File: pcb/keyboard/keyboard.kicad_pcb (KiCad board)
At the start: 2 copper layers, 125.5 x 94.2 mm, 62 parts

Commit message: imp: pcb design change
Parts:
- added REF**: TC24CA, Button_Switch_SMD:TC24CA, F.Cu at (259.1, 106.5)
- added REF**: TC24CA, Button_Switch_SMD:TC24CA, B.Cu at (259.1, 106.5)
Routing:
- net P7: track 17.5 -> 24.8 mm, vias 1 -> 2
- net P9: track 58.1 -> 54.4 mm
- net GND: track 95.3 -> 96.9 mm
- net BAT: track 70.6 -> 70.9 mm, vias 3 -> 5

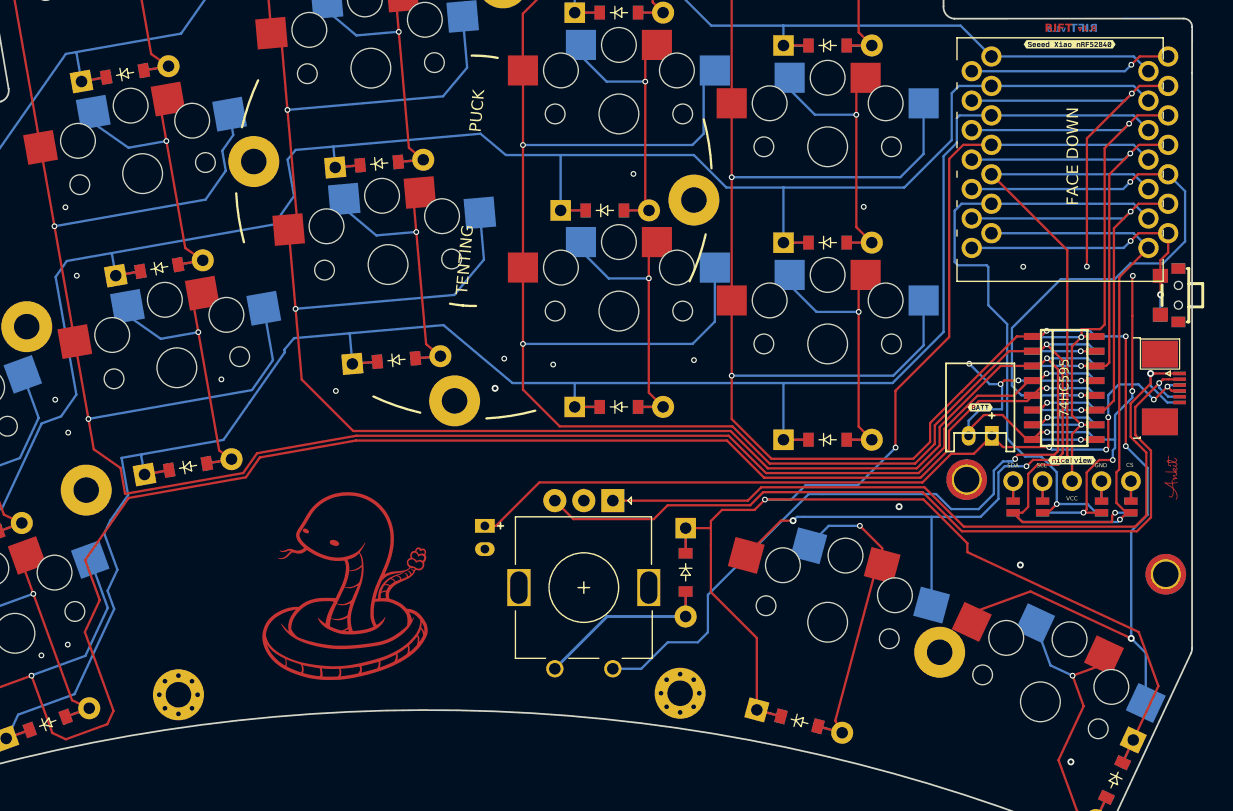
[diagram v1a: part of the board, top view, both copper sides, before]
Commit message: add: i2c resistor pull resistor
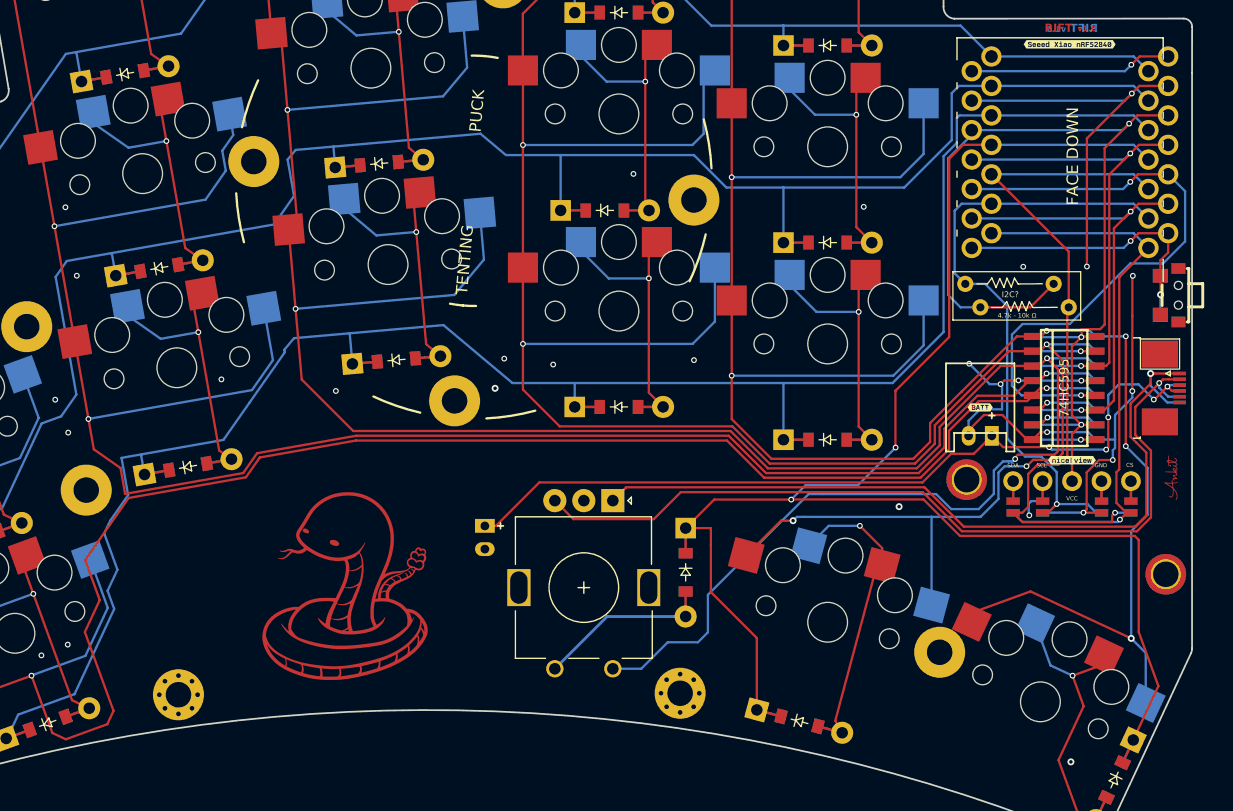
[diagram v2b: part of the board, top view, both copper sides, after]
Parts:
- added REF**: R_Axial_DIN0204_L3.6mm_D1.6mm_P7.62mm_Horizontal, Resistor_THT:R_Axial_DIN0204_L3.6mm_D1.6mm_P7.62mm_Horizontal, F.Cu at (241.4, 105.5)
- added REF**: 4.5k, Resistor_THT:R_Axial_DIN0204_L3.6mm_D1.6mm_P7.62mm_Horizontal, B.Cu at (250.4, 107.5)
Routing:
- net VCC: track 63.1 -> 88.2 mm
- net P3: track 142.8 -> 147.9 mm
- net SCL: track 3.44 -> 5.75 mm, vias 0 -> 1
- net GND: track 96.9 -> 95.9 mm, vias 37 -> 36
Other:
- board text added: "4.7k - 10k Ω"
- board text added: "I2C?"

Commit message: add: i2c pull-up resistors and name on silkscreen
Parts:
- removed the G*** at (259.5, 122.3) (x2)
- added G*** (x2): LOGO, GraphicsKicad:signature_large, F.Cu at (248.2, 130.9)
- added G*** (x2): LOGO, GraphicsKicad:signature_large, B.Cu at (248.4, 130.8)
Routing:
- net Q1: track 198.6 -> 198.0 mm
- net GND: vias 36 -> 39
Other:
- board text added: "F"
- board text added: "I"
- board text added: "R"
- board text added: "T"
